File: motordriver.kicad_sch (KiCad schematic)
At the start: 56 parts, among them Q401 STP15810, Q402 STP15810, Q403 STP15810, Q404 STP15810, Q405 STP15810, Q406 STP15810, Q407 STP15810, Q408 STP15810, Q409 STP15810, Q410 STP15810, Q411 STP15810, Q412 STP15810, U401 LM5110-1MX, U402 LM5110-1MX, U403 LM5110-1MX, U404 LM5110-1MX, U405 LM5110-1MX, U406 LM5110-1MX

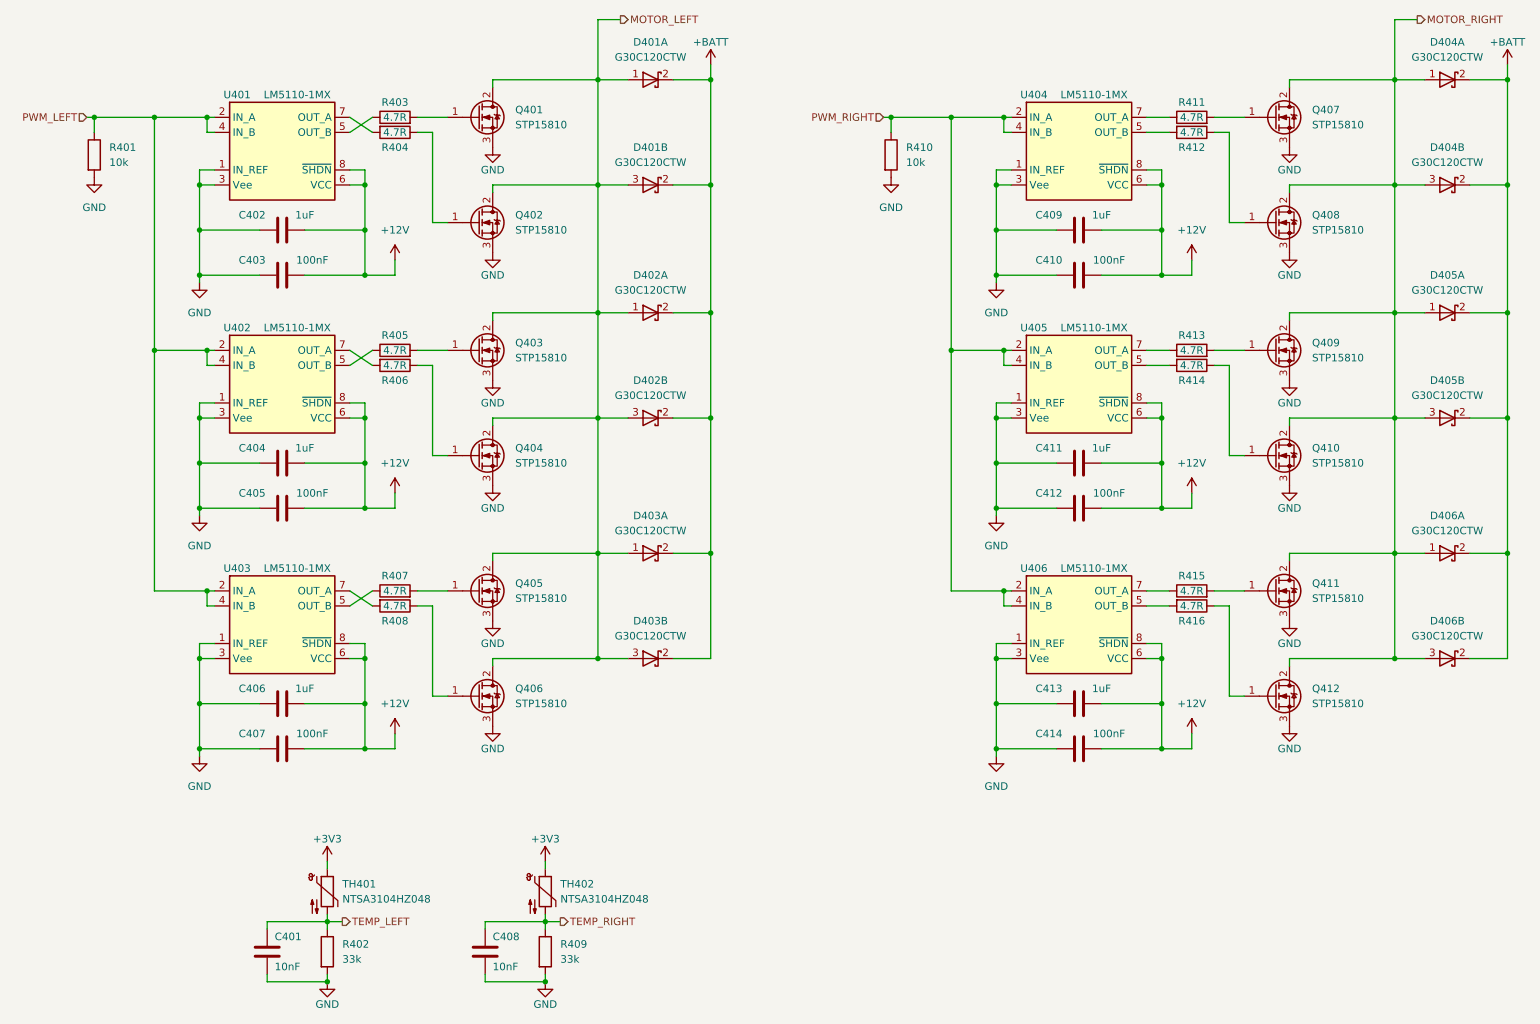
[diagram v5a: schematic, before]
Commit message: Swap for isolated TO220 diodes
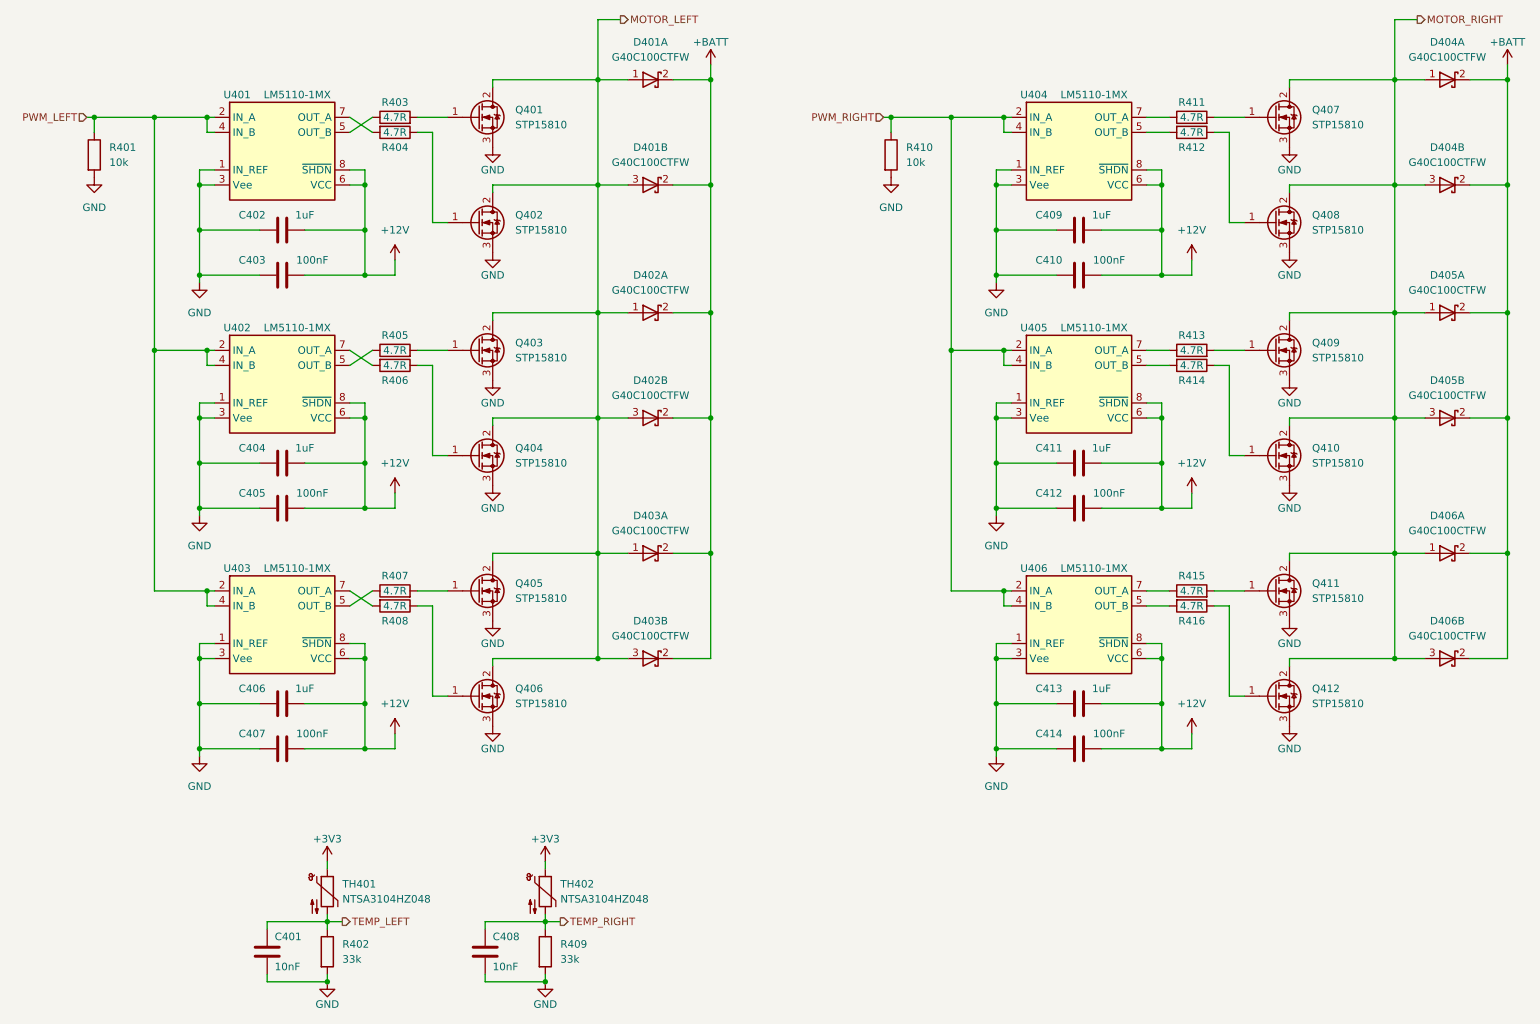
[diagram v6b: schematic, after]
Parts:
- D401, D402, D403, D404, D405, D406: value G30C120CTW -> G40C100CTFW
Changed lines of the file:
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@@
     (in_bom yes) (on_board yes) (fields_autoplaced)
     (property "Reference" "D401" (id 0) (at 121.92 27.94 0))
-    (property "Value" "G30C120CTW" (id 1) (at 121.92 30.48 0))
+    (property "Value" "G40C100CTFW" (id 1) (at 121.92 30.48 0))
     (property "Footprint" "Package_TO_SOT_THT:TO-220-3_Vertical" (id 2) (at 121.92 21.59 0)
       (effects (font (size 1.27 1.27)) hide)
@@
     (in_bom yes) (on_board yes) (fields_autoplaced)
     (property "Reference" "D401" (id 0) (at 121.92 45.72 0))
-    (property "Value" "G30C120CTW" (id 1) (at 121.92 48.26 0))
+    (property "Value" "G40C100CTFW" (id 1) (at 121.92 48.26 0))
     (property "Footprint" "Package_TO_SOT_THT:TO-220-3_Vertical" (id 2) (at 121.92 39.37 0)
       (effects (font (size 1.27 1.27)) hide)
@@
     (in_bom yes) (on_board yes) (fields_autoplaced)
     (property "Reference" "D402" (id 0) (at 121.92 67.31 0))
-    (property "Value" "G30C120CTW" (id 1) (at 121.92 69.85 0))
+    (property "Value" "G40C100CTFW" (id 1) (at 121.92 69.85 0))
     (property "Footprint" "Package_TO_SOT_THT:TO-220-3_Vertical" (id 2) (at 121.92 60.96 0)
       (effects (font (size 1.27 1.27)) hide)
@@
     (in_bom yes) (on_board yes) (fields_autoplaced)
     (property "Reference" "D402" (id 0) (at 121.92 85.09 0))
-    (property "Value" "G30C120CTW" (id 1) (at 121.92 87.63 0))
+    (property "Value" "G40C100CTFW" (id 1) (at 121.92 87.63 0))
     (property "Footprint" "Package_TO_SOT_THT:TO-220-3_Vertical" (id 2) (at 121.92 78.74 0)
       (effects (font (size 1.27 1.27)) hide)
@@
     (in_bom yes) (on_board yes) (fields_autoplaced)
     (property "Reference" "D403" (id 0) (at 121.92 107.95 0))
-    (property "Value" "G30C120CTW" (id 1) (at 121.92 110.49 0))
+    (property "Value" "G40C100CTFW" (id 1) (at 121.92 110.49 0))
     (property "Footprint" "Package_TO_SOT_THT:TO-220-3_Vertical" (id 2) (at 121.92 101.6 0)
       (effects (font (size 1.27 1.27)) hide)
@@
     (in_bom yes) (on_board yes) (fields_autoplaced)
     (property "Reference" "D403" (id 0) (at 121.92 125.73 0))
-    (property "Value" "G30C120CTW" (id 1) (at 121.92 128.27 0))
+    (property "Value" "G40C100CTFW" (id 1) (at 121.92 128.27 0))
     (property "Footprint" "Package_TO_SOT_THT:TO-220-3_Vertical" (id 2) (at 121.92 119.38 0)
       (effects (font (size 1.27 1.27)) hide)
@@
     (in_bom yes) (on_board yes) (fields_autoplaced)
     (property "Reference" "D404" (id 0) (at 256.54 27.94 0))
-    (property "Value" "G30C120CTW" (id 1) (at 256.54 30.48 0))
+    (property "Value" "G40C100CTFW" (id 1) (at 256.54 30.48 0))
     (property "Footprint" "Package_TO_SOT_THT:TO-220-3_Vertical" (id 2) (at 256.54 21.59 0)
       (effects (font (size 1.27 1.27)) hide)
@@
     (in_bom yes) (on_board yes) (fields_autoplaced)
     (property "Reference" "D404" (id 0) (at 256.54 45.72 0))
-    (property "Value" "G30C120CTW" (id 1) (at 256.54 48.26 0))
+    (property "Value" "G40C100CTFW" (id 1) (at 256.54 48.26 0))
     (property "Footprint" "Package_TO_SOT_THT:TO-220-3_Vertical" (id 2) (at 256.54 39.37 0)
       (effects (font (size 1.27 1.27)) hide)
@@
     (in_bom yes) (on_board yes) (fields_autoplaced)
     (property "Reference" "D405" (id 0) (at 256.54 67.31 0))
-    (property "Value" "G30C120CTW" (id 1) (at 256.54 69.85 0))
+    (property "Value" "G40C100CTFW" (id 1) (at 256.54 69.85 0))
     (property "Footprint" "Package_TO_SOT_THT:TO-220-3_Vertical" (id 2) (at 256.54 60.96 0)
       (effects (font (size 1.27 1.27)) hide)
@@
     (in_bom yes) (on_board yes) (fields_autoplaced)
     (property "Reference" "D405" (id 0) (at 256.54 85.09 0))
-    (property "Value" "G30C120CTW" (id 1) (at 256.54 87.63 0))
+    (property "Value" "G40C100CTFW" (id 1) (at 256.54 87.63 0))
     (property "Footprint" "Package_TO_SOT_THT:TO-220-3_Vertical" (id 2) (at 256.54 78.74 0)
       (effects (font (size 1.27 1.27)) hide)
@@
     (in_bom yes) (on_board yes) (fields_autoplaced)
     (property "Reference" "D406" (id 0) (at 256.54 107.95 0))
-    (property "Value" "G30C120CTW" (id 1) (at 256.54 110.49 0))
+    (property "Value" "G40C100CTFW" (id 1) (at 256.54 110.49 0))
     (property "Footprint" "Package_TO_SOT_THT:TO-220-3_Vertical" (id 2) (at 256.54 101.6 0)
       (effects (font (size 1.27 1.27)) hide)
@@
     (in_bom yes) (on_board yes) (fields_autoplaced)
     (property "Reference" "D406" (id 0) (at 256.54 125.73 0))
-    (property "Value" "G30C120CTW" (id 1) (at 256.54 128.27 0))
+    (property "Value" "G40C100CTFW" (id 1) (at 256.54 128.27 0))
     (property "Footprint" "Package_TO_SOT_THT:TO-220-3_Vertical" (id 2) (at 256.54 119.38 0)
       (effects (font (size 1.27 1.27)) hide)
